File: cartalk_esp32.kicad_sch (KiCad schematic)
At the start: 24 parts, among them IC1 CP2104, Q1 mmbt2222, Q2 mmbt2222, SW2 KMR2, U1 HUB75 Connector Female, U2 AP2112-3.3, X2 ESP32_WROOM32_SKINNY, X4 20329

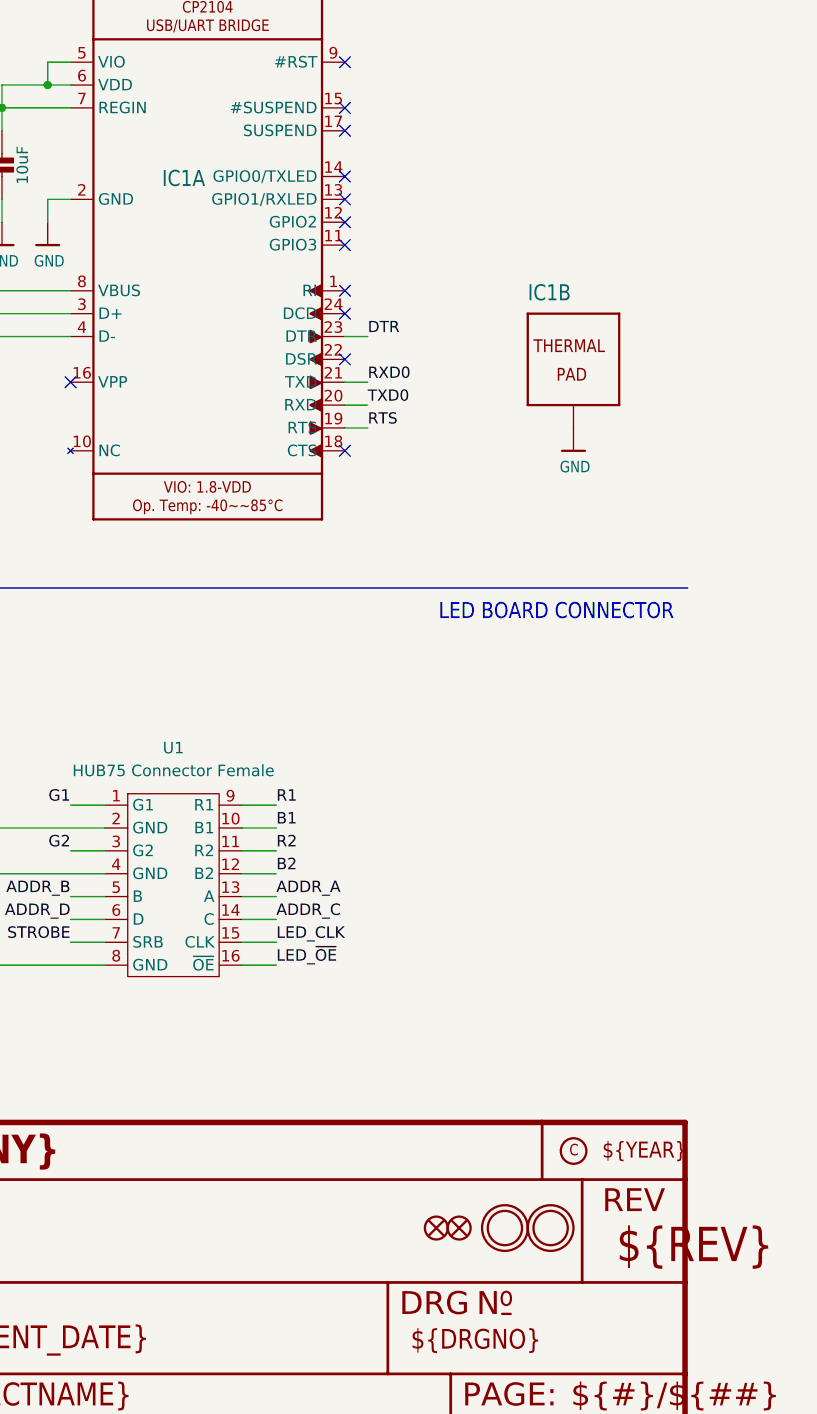
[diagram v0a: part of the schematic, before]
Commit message: First pass of footprint assignments complete.
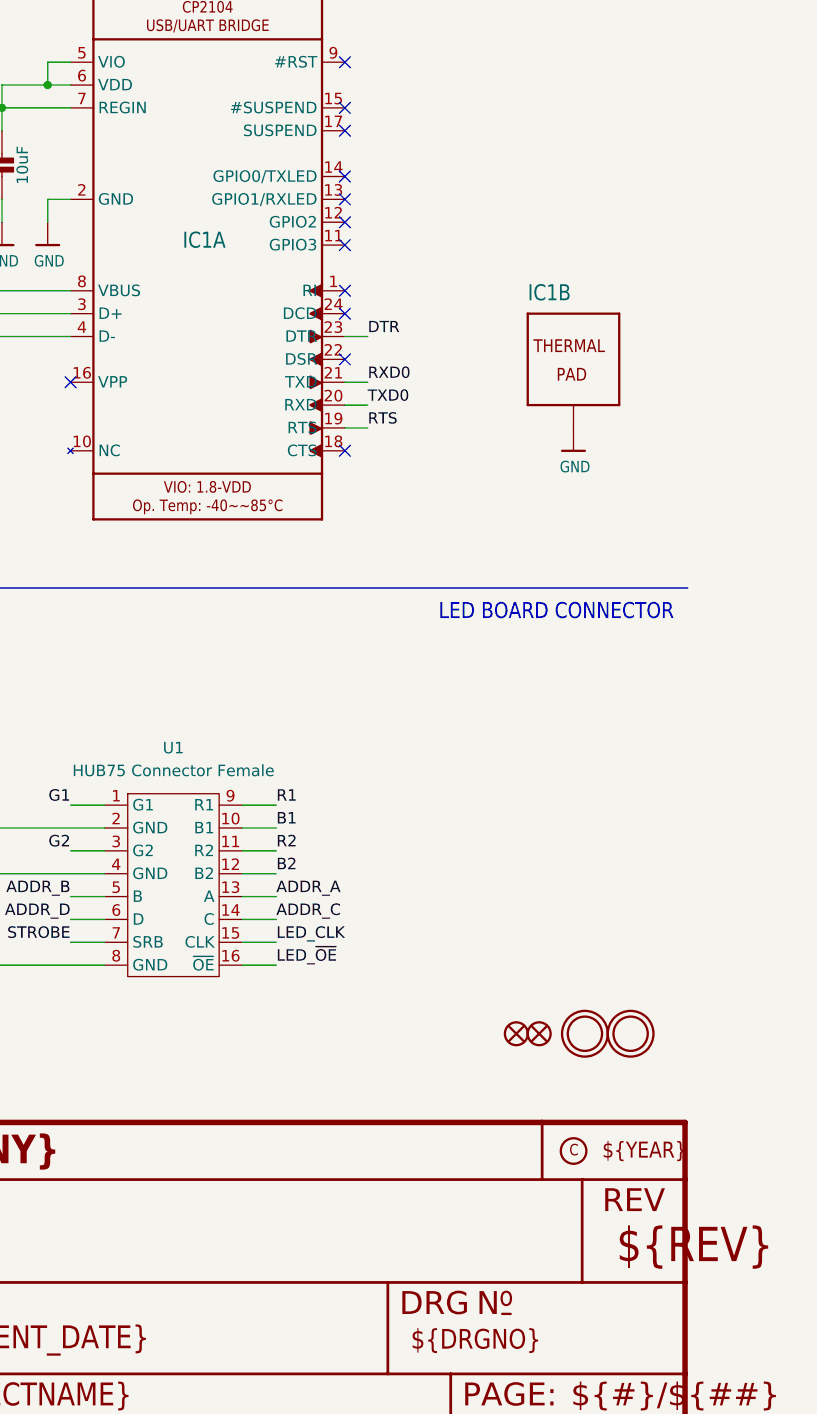
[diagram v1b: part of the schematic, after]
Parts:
- D3: footprint cartalk_esp32:CHIPLED_0805_NOOUTLINE -> LED_SMD:LED_0603_1608Metric
- D4: footprint cartalk_esp32:SOD-123 -> Diode_SMD:D_SOD-123
- IC1: footprint cartalk_esp32:QFN24_4MM_SMSC -> CP2104:QFN50P400X400X80-25N
- R10, R12, R7: footprint cartalk_esp32:0603-NO -> Resistor_SMD:R_0603_1608Metric
- R13: footprint cartalk_esp32:RESPACK_4X0603 -> Resistor_SMD:R_Array_Convex_4x0603
- SW2: footprint cartalk_esp32:BTN_KMR2_4.6X2.8 -> smd_button:PTS645SL43SMTR92LFS_CNK-L
- U$31, U$32: footprint cartalk_esp32:MOUNTINGHOLE_2.5_PLATED -> MountingHole:MountingHole_2.5mm_Pad
- U$34, U$35: footprint cartalk_esp32:FIDUCIAL_1MM -> Fiducial:Fiducial_1mm_Mask2mm
- U2: footprint cartalk_esp32:SOT23-5 -> Package_TO_SOT_SMD:SOT-23-5
- X2: footprint cartalk_esp32:WROOM32_SKINNY -> RF_Module:ESP32-WROOM-32
- X4: footprint cartalk_esp32:4UCONN_20329_V2 -> smd_usb_micro_b_connector:CONN_10118192-0002LF_AMP
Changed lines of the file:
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@@
 	(symbol
 		(lib_id "cartalk_esp32-eagle-import:FIDUCIAL_1MM")
-		(at 248.92 172.72 0)
+		(at 257.81 151.13 0)
 		(unit 1)
 		(exclude_from_sim no)
@@
 		(dnp no)
 		(property "Reference" "U$34"
-			(at 248.92 172.72 0)
+			(at 257.81 151.13 0)
 			(effects
 				(font
@@
 		)
 		(property "Value" "FIDUCIAL_1MM"
-			(at 248.92 172.72 0)
+			(at 257.81 151.13 0)
 			(effects
 				(font
@@
 			)
 		)
-		(property "Footprint" "cartalk_esp32:FIDUCIAL_1MM"
-			(at 248.92 172.72 0)
+		(property "Footprint" "Fiducial:Fiducial_1mm_Mask2mm"
+			(at 257.81 151.13 0)
 			(effects
 				(font
@@
 		)
 		(property "Datasheet" ""
-			(at 248.92 172.72 0)
+			(at 257.81 151.13 0)
 			(effects
 				(font
@@
 		)
 		(property "Description" ""
-			(at 248.92 172.72 0)
+			(at 257.81 151.13 0)
 			(effects
 				(font
@@
 			)
 		)
-		(property "Footprint" "cartalk_esp32:RESPACK_4X0603"
+		(property "Footprint" "Resistor_SMD:R_Array_Convex_4x0603"
 			(at 127 118.11 0)
 			(effects
@@
 			)
 		)
-		(property "Footprint" "cartalk_esp32:SOT23-5"
+		(property "Footprint" "Package_TO_SOT_SMD:SOT-23-5"
 			(at 68.58 45.72 0)
 			(effects
@@
 			)
 		)
-		(property "Footprint" "cartalk_esp32:WROOM32_SKINNY"
+		(property "Footprint" "RF_Module:ESP32-WROOM-32"
 			(at 68.58 114.3 0)
 			(effects
@@
 	(symbol
 		(lib_id "cartalk_esp32-eagle-import:MOUNTINGHOLE2.5")
-		(at 259.08 172.72 0)
+		(at 267.97 151.13 0)
 		(unit 1)
 		(exclude_from_sim no)
@@
 		(dnp no)
 		(property "Reference" "U$32"
-			(at 259.08 172.72 0)
+			(at 267.97 151.13 0)
 			(effects
 				(font
@@
 		)
 		(property "Value" "MOUNTINGHOLE2.5"
-			(at 259.08 172.72 0)
+			(at 267.97 151.13 0)
 			(effects
 				(font
@@
 			)
 		)
-		(property "Footprint" "cartalk_esp32:MOUNTINGHOLE_2.5_PLATED"
-			(at 259.08 172.72 0)
+		(property "Footprint" "MountingHole:MountingHole_2.5mm_Pad"
+			(at 267.97 151.13 0)
 			(effects
 				(font
@@
 		)
 		(property "Datasheet" ""
-			(at 259.08 172.72 0)
+			(at 267.97 151.13 0)
 			(effects
 				(font
@@
 		)
 		(property "Description" ""
-			(at 259.08 172.72 0)
+			(at 267.97 151.13 0)
 			(effects
 				(font
@@
 			)
 		)
-		(property "Footprint" "cartalk_esp32:0603-NO"
+		(property "Footprint" "Resistor_SMD:R_0603_1608Metric"
 			(at 139.7 177.8 0)
 			(effects
@@
 			)
 		)
-		(property "Footprint" "cartalk_esp32:4UCONN_20329_V2"
+		(property "Footprint" "smd_usb_micro_b_connector:CONN_10118192-0002LF_AMP"
 			(at 175.26 73.66 0)
 			(effects
@@
 		(dnp no)
 		(property "Reference" "IC1"
-			(at 215.9 57.15 0)
+			(at 218.186 64.008 0)
 			(effects
 				(font
@@
 			)
 		)
-		(property "Footprint" "cartalk_esp32:QFN24_4MM_SMSC"
+		(property "Footprint" "CP2104:QFN50P400X400X80-25N"
 			(at 220.98 63.5 0)
 			(effects
@@
 			)
 		)
-		(property "Footprint" "cartalk_esp32:SOD-123"
+		(property "Footprint" "Diode_SMD:D_SOD-123"
 			(at 36.83 43.18 0)
 			(effects
@@
 	(symbol
 		(lib_id "cartalk_esp32-eagle-import:MOUNTINGHOLE2.5")
-		(at 254 172.72 0)
+		(at 262.89 151.13 0)
 		(unit 1)
 		(exclude_from_sim no)
@@
 		(dnp no)
 		(property "Reference" "U$31"
-			(at 254 172.72 0)
+			(at 262.89 151.13 0)
 			(effects
 				(font
@@
 		)
 		(property "Value" "MOUNTINGHOLE2.5"
-			(at 254 172.72 0)
+			(at 262.89 151.13 0)
 			(effects
 				(font
@@
 			)
 		)
-		(property "Footprint" "cartalk_esp32:MOUNTINGHOLE_2.5_PLATED"
-			(at 254 172.72 0)
+		(property "Footprint" "MountingHole:MountingHole_2.5mm_Pad"
+			(at 262.89 151.13 0)
 			(effects
 				(font
@@
 		)
 		(property "Datasheet" ""
-			(at 254 172.72 0)
+			(at 262.89 151.13 0)
 			(effects
 				(font
@@
 		)
 		(property "Description" ""
-			(at 254 172.72 0)
+			(at 262.89 151.13 0)
 			(effects
 				(font
@@
 			)
 		)
-		(property "Footprint" "cartalk_esp32:BTN_KMR2_4.6X2.8"
+		(property "Footprint" "smd_button:PTS645SL43SMTR92LFS_CNK-L"
 			(at 139.7 53.34 0)
 			(effects
@@
 	(symbol
 		(lib_id "cartalk_esp32-eagle-import:FIDUCIAL_1MM")
-		(at 246.38 172.72 0)
+		(at 255.27 151.13 0)
 		(unit 1)
 		(exclude_from_sim no)
@@
 		(dnp no)
 		(property "Reference" "U$35"
-			(at 246.38 172.72 0)
+			(at 255.27 151.13 0)
 			(effects
 				(font
@@
 		)
 		(property "Value" "FIDUCIAL_1MM"
-			(at 246.38 172.72 0)
+			(at 255.27 151.13 0)
 			(effects
 				(font
@@
 			)
 		)
-		(property "Footprint" "cartalk_esp32:FIDUCIAL_1MM"
-			(at 246.38 172.72 0)
+		(property "Footprint" "Fiducial:Fiducial_1mm_Mask2mm"
+			(at 255.27 151.13 0)
 			(effects
 				(font
@@
 		)
 		(property "Datasheet" ""
-			(at 246.38 172.72 0)
+			(at 255.27 151.13 0)
 			(effects
 				(font
@@
 		)
 		(property "Description" ""
-			(at 246.38 172.72 0)
+			(at 255.27 151.13 0)
 			(effects
 				(font
@@
 			)
 		)
-		(property "Footprint" "cartalk_esp32:0603-NO"
+		(property "Footprint" "Resistor_SMD:R_0603_1608Metric"
 			(at 27.94 50.8 0)
 			(effects
@@
 			)
 		)
-		(property "Footprint" "cartalk_esp32:QFN24_4MM_SMSC"
+		(property "Footprint" "CP2104:QFN50P400X400X80-25N"
 			(at 261.62 76.2 0)
 			(effects
@@
 			)
 		)
-		(property "Footprint" "cartalk_esp32:RESPACK_4X0603"
+		(property "Footprint" "Resistor_SMD:R_Array_Convex_4x0603"
 			(at 142.24 35.56 0)
 			(effects
@@
 			)
 		)
-		(property "Footprint" "cartalk_esp32:RESPACK_4X0603"
+		(property "Footprint" "Resistor_SMD:R_Array_Convex_4x0603"
 			(at 127 100.33 0)
 			(effects
@@
 			)
 		)
-		(property "Footprint" "cartalk_esp32:CHIPLED_0805_NOOUTLINE"
+		(property "Footprint" "LED_SMD:LED_0603_1608Metric"
 			(at 139.7 167.64 0)
 			(effects
@@
 			)
 		)
-		(property "Footprint" "cartalk_esp32:0603-NO"
+		(property "Footprint" "Resistor_SMD:R_0603_1608Metric"
 			(at 53.34 48.26 0)
 			(effects

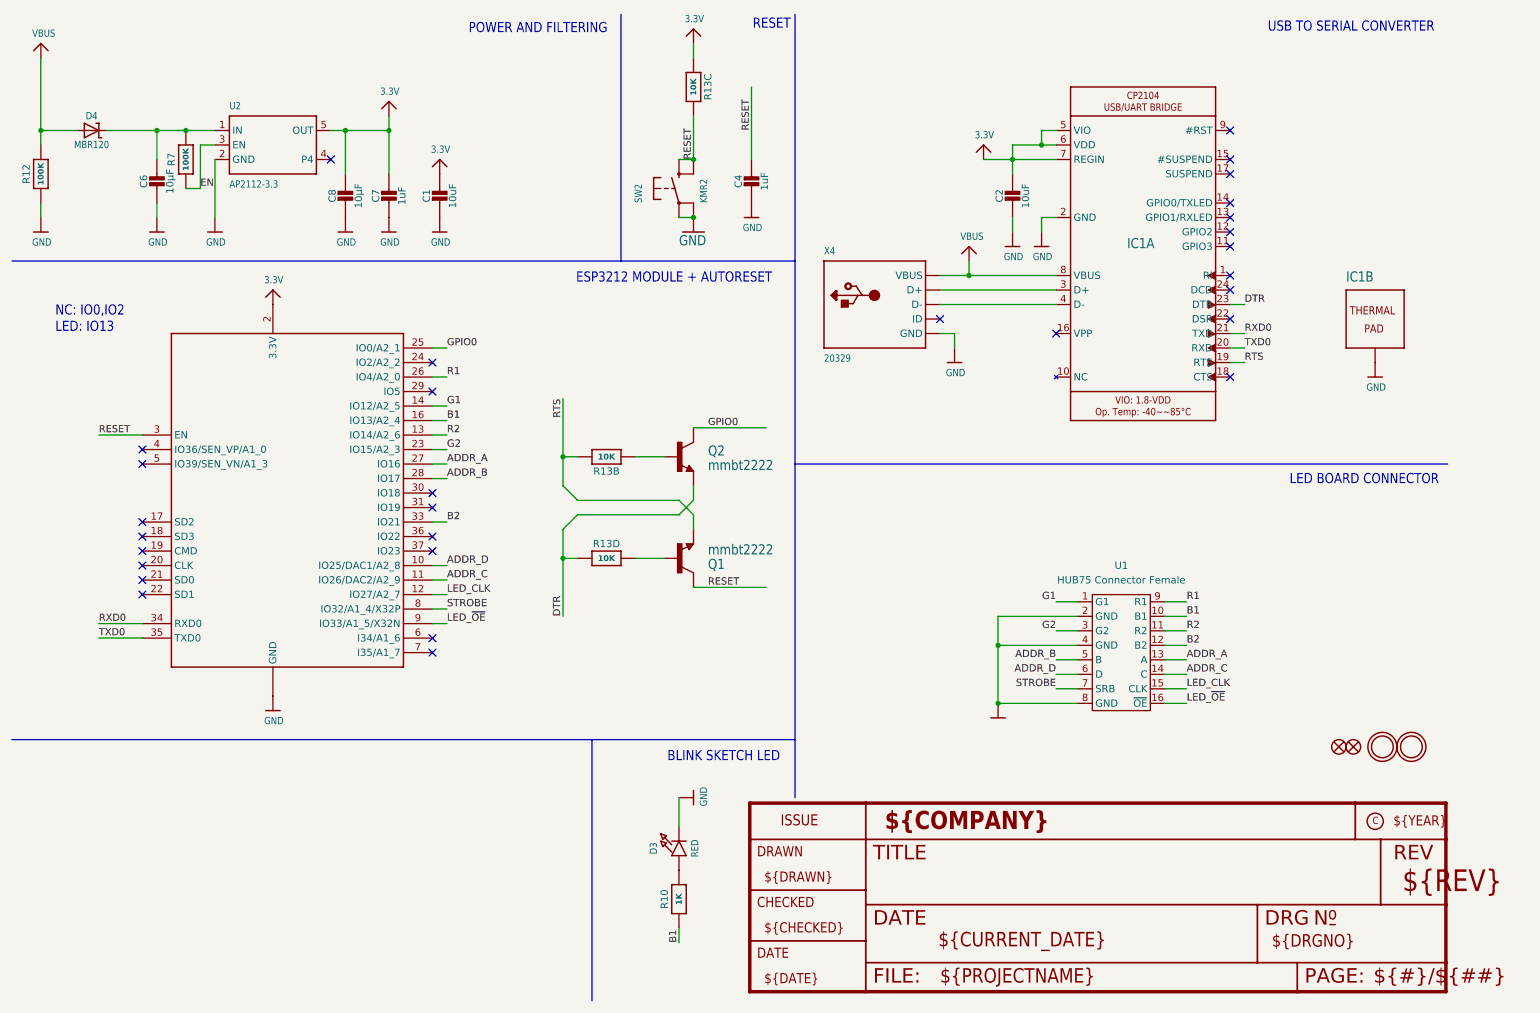
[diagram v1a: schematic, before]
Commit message: Fix USB footprint to match pin names of symbol.
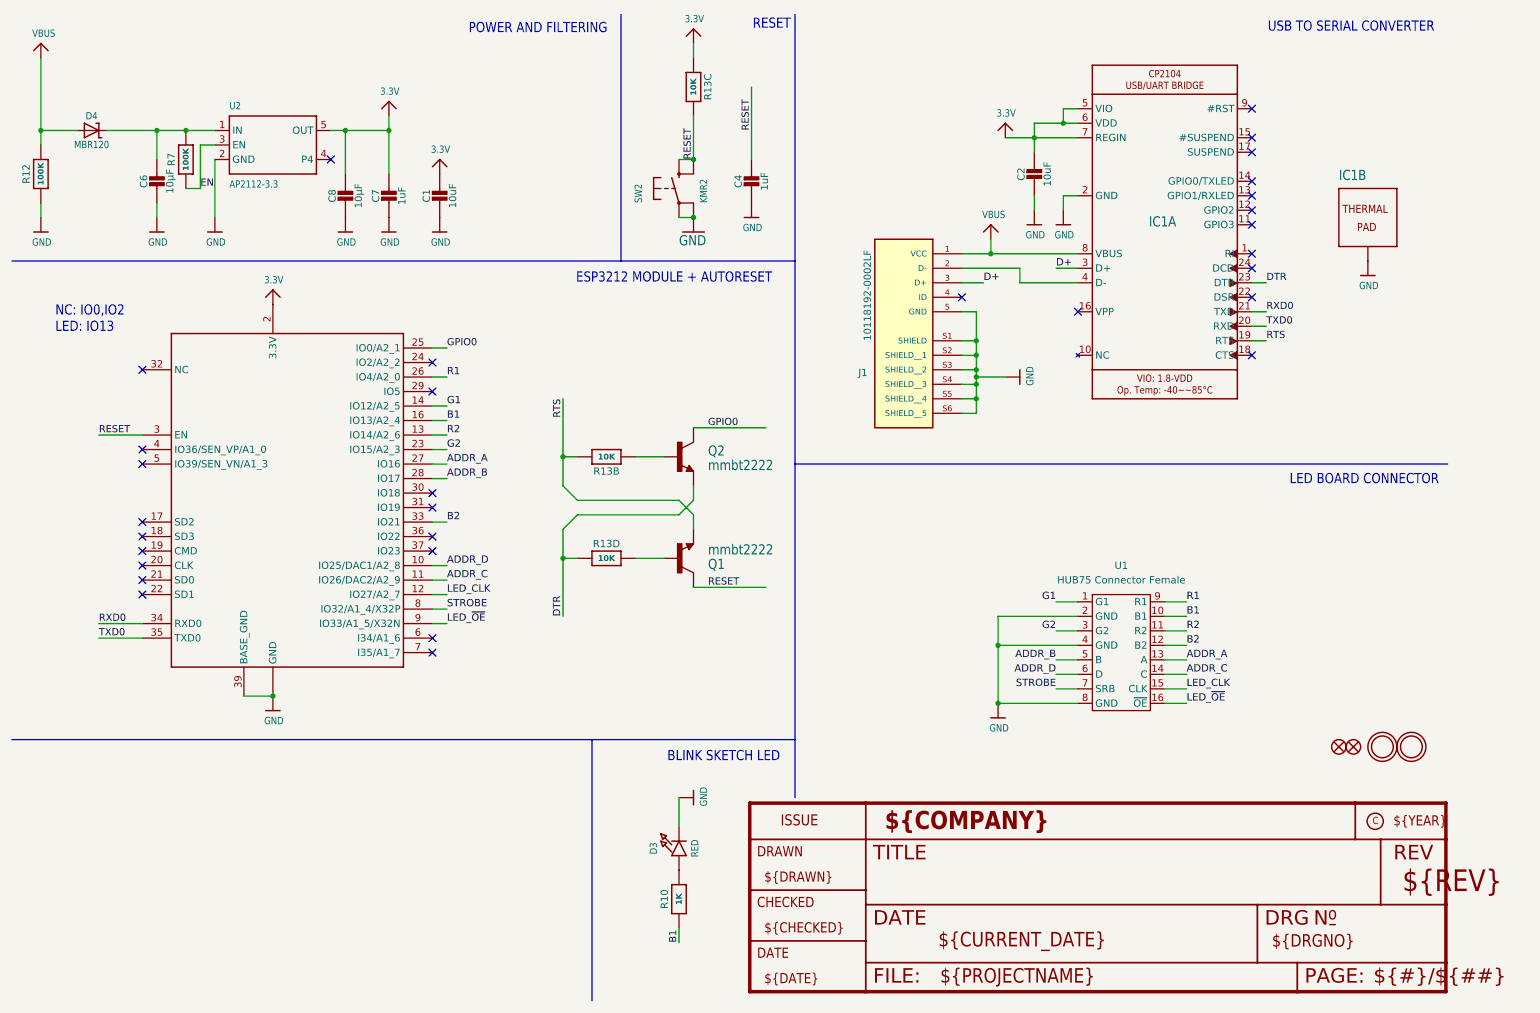
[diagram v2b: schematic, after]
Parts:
- removed X4: 20329, smd_usb_micro_b_connector:CONN_10118192-0002LF_AMP, symbol cartalk_esp32-eagle-import:USB_MICRO_20329_V2
- added J1: 10118192-0002LF, smd_usb_micro_b_connector:CONN_10118192-0002LF_AMP, symbol 10118192-0002LF:10118192-0002LF
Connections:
- net GND: now also U1.2 (GND), U1.4 (GND), U1.8 (GND), X2.39 (BASE_GND), J1.5 (GND), J1.S1 (SHIELD), J1.S2 (SHIELD__1), J1.S3 (SHIELD__2), J1.S4 (SHIELD__3), J1.S5 (SHIELD__4), J1.S6 (SHIELD__5)
- net VBUS: now also J1.1 (VCC)
- net D+: now reaches IC1.3 (D+)
- net D+: now also J1.3 (D+)
- net at IC1.4 (D-): now also J1.2 (D-)
- no-connect marks 30 -> 31
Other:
- moved on the sheet: C2, IC1A, IC1B
